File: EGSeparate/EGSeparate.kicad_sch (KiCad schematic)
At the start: 3 parts, among them IC1 PIC16F15325-I_P, IC2 MCP6232-E_P, U1 Opamp_Dual

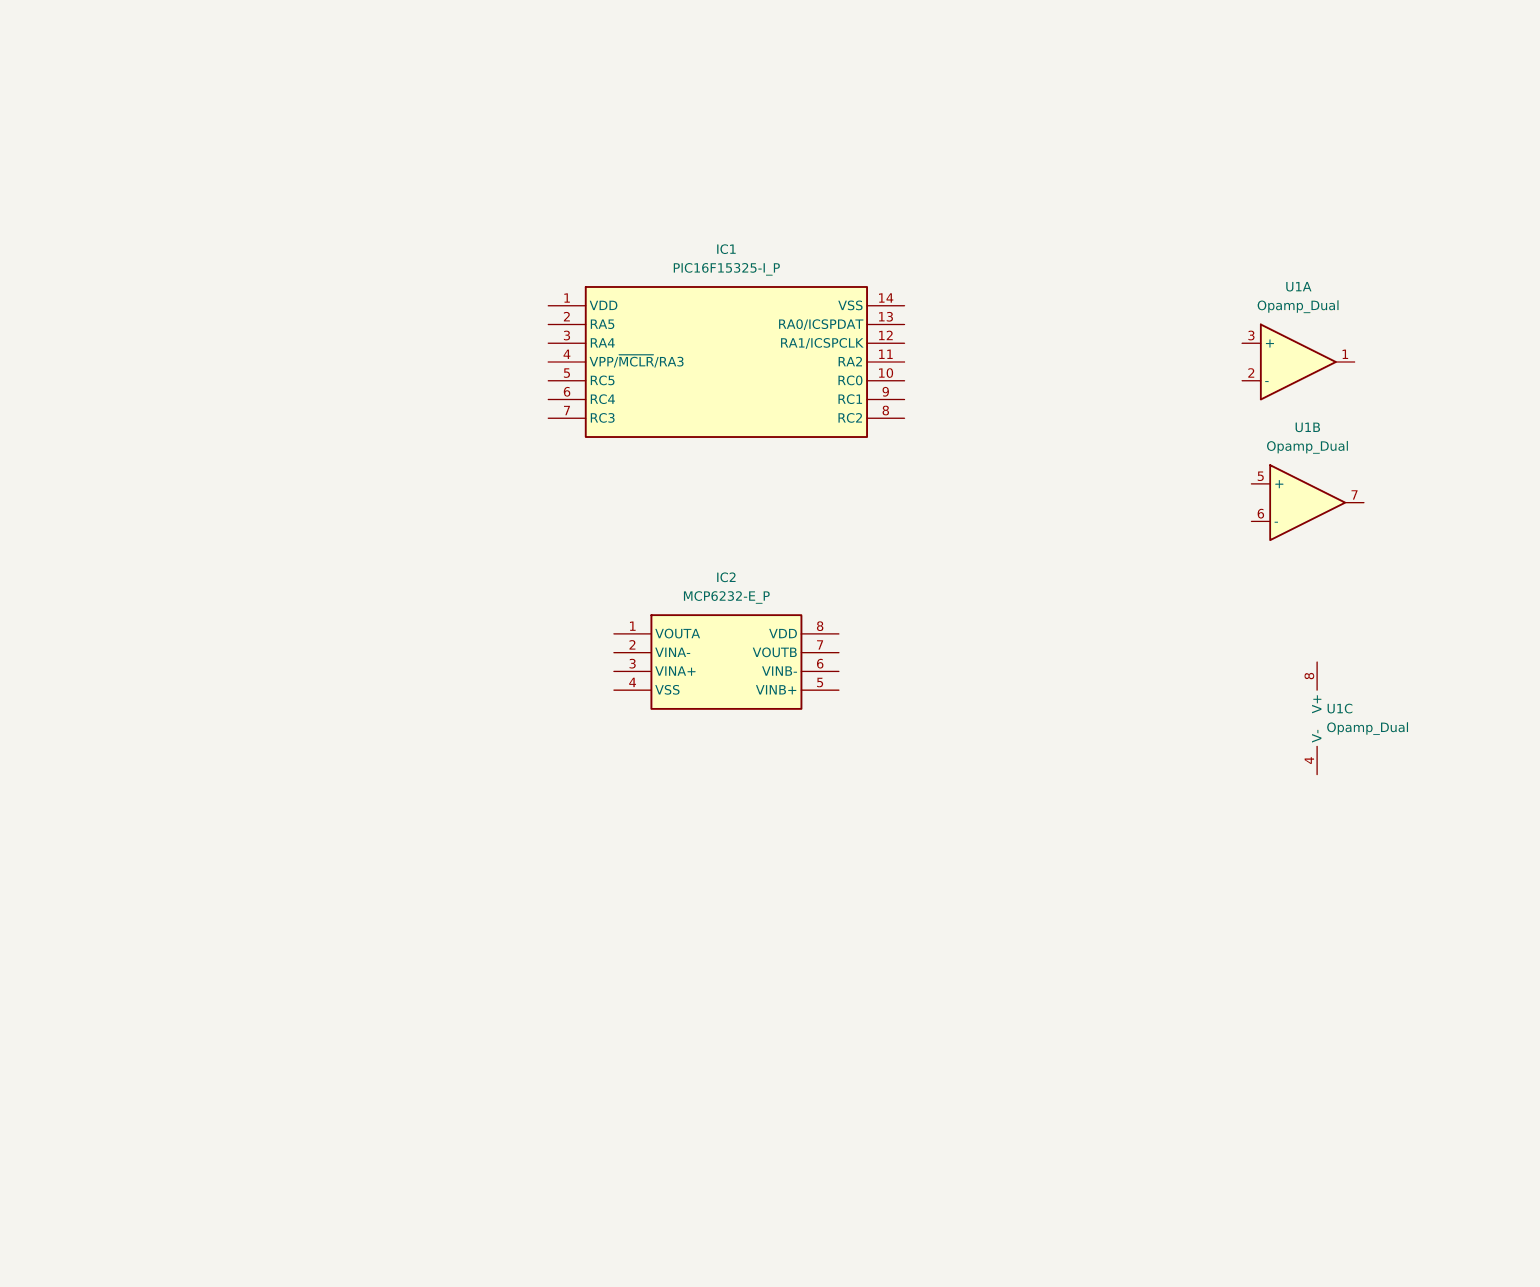
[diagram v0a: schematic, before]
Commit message: LFOSeparate
LFOSeparateは配線完了
EGSeparateは回路図作成中
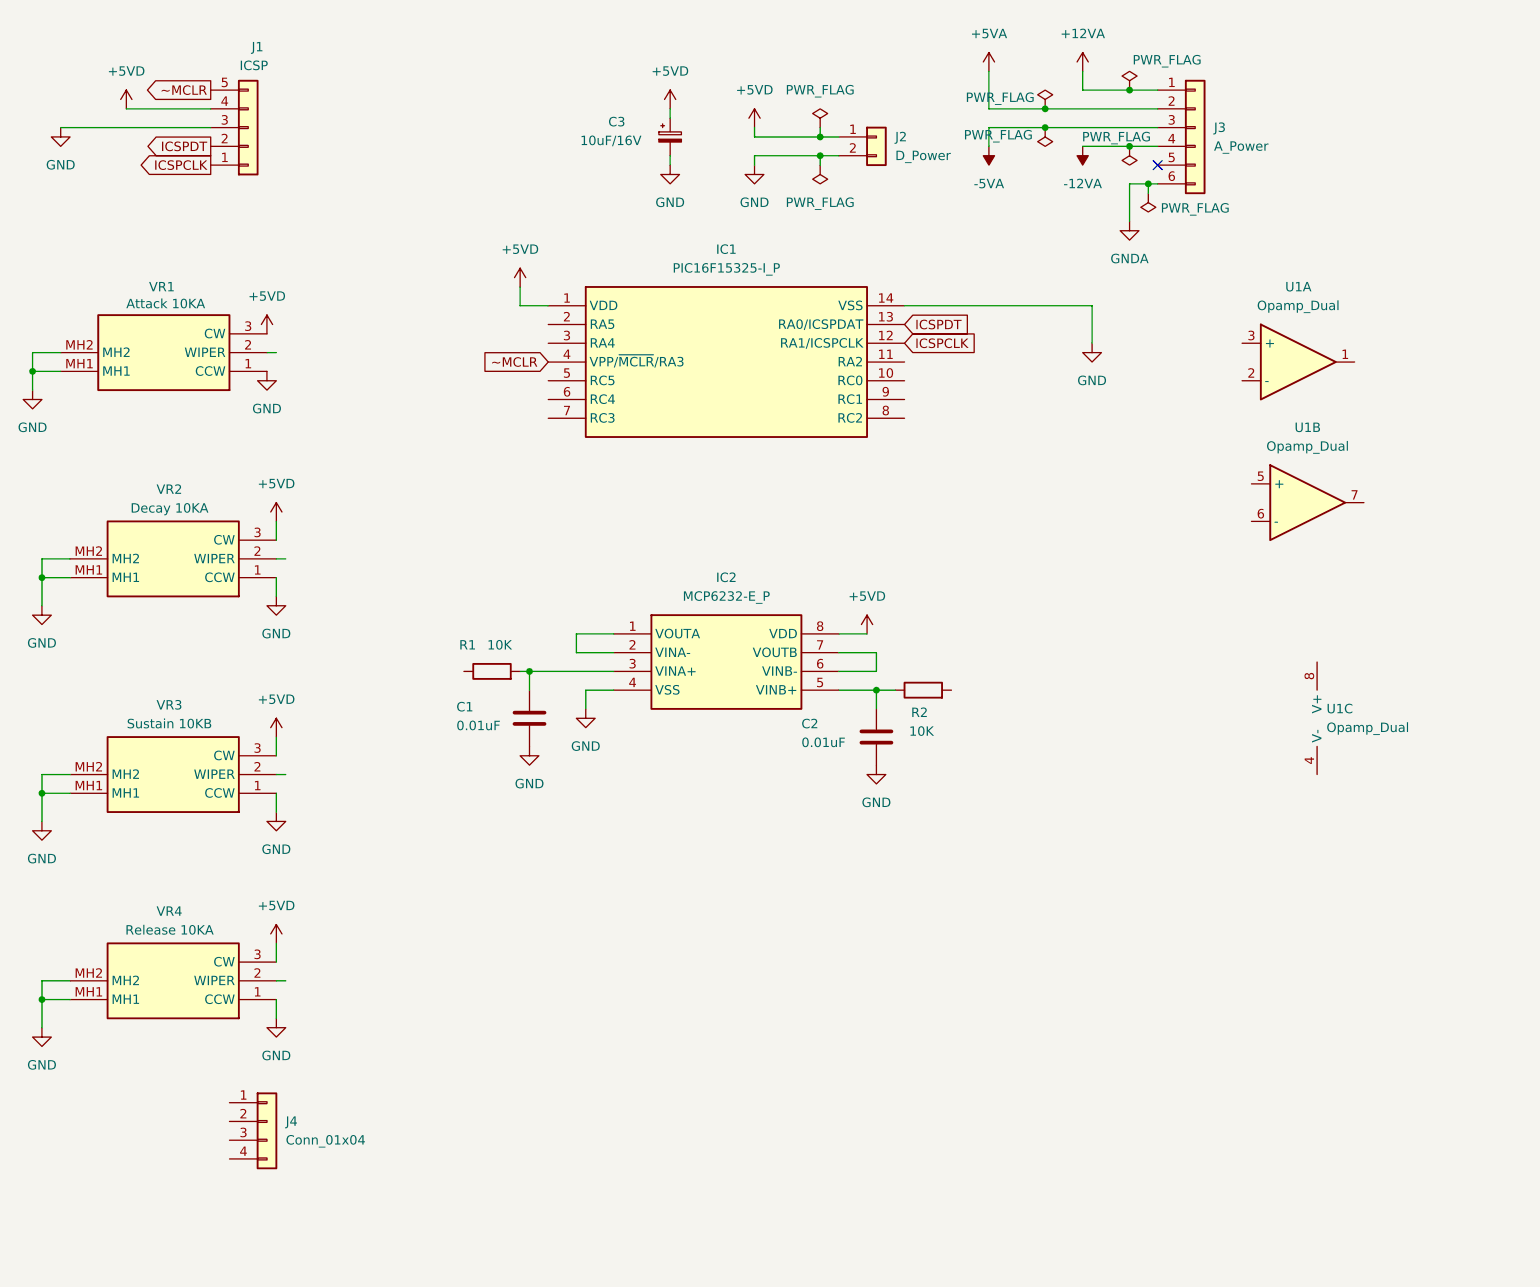
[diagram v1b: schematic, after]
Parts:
- added C1, C2: 0.01uF, Capacitor_THT:C_Disc_D3.4mm_W2.1mm_P2.50mm, symbol Device:C
- added C3: 10uF/16V, Capacitor_THT:CP_Radial_D5.0mm_P2.50mm, symbol Device:C_Polarized_Small
- added J1: ICSP, Connector_PinHeader_2.54mm:PinHeader_1x05_P2.54mm_Horizontal, symbol Connector_Generic:Conn_01x05
- added J2: D_Power, Connector_PinSocket_2.54mm:PinSocket_1x02_P2.54mm_Vertical, symbol Connector_Generic:Conn_01x02
- added J3: A_Power, Connector_PinHeader_2.54mm:PinHeader_1x06_P2.54mm_Vertical, symbol Connector_Generic:Conn_01x06
- added J4: Conn_01x04, Connector_PinHeader_2.54mm:PinHeader_1x04_P2.54mm_Vertical, symbol Connector_Generic:Conn_01x04
- added R1, R2: 10K, Resistor_THT:R_Axial_DIN0204_L3.6mm_D1.6mm_P2.54mm_Vertical, symbol Device:R
- added VR1: Attack 10KA, SamacSys_Parts:RK09D117000B, symbol SamacSys_Parts:RK09D117000B
- added VR2: Decay 10KA, SamacSys_Parts:RK09D117000B, symbol SamacSys_Parts:RK09D117000B
- added VR3: Sustain 10KB, SamacSys_Parts:RK09D117000B, symbol SamacSys_Parts:RK09D117000B
- added VR4: Release 10KA, SamacSys_Parts:RK09D117000B, symbol SamacSys_Parts:RK09D117000B
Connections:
- net at IC2.1 (VOUTA): now also IC2.2 (VINA-)
- net at IC2.3 (VINA+): now also C1.1, R1.2
- net GND: now reaches IC2.4 (VSS)
- net GND: now also IC1.14 (VSS), C1.2, C2.2, C3.2, J1.3 (Pin_3), J2.2 (Pin_2), VR1.1 (CCW), VR1.MH1, VR1.MH2, VR2.1 (CCW), VR2.MH1, VR2.MH2, VR3.1 (CCW), VR3.MH1, VR3.MH2, VR4.1 (CCW), VR4.MH1, VR4.MH2
- net at IC2.5 (VINB+): now also C2.1, R2.1
- net at IC2.6 (VINB-): now also IC2.7 (VOUTB)
- net +5VD: now reaches IC2.8 (VDD)
- net +5VD: now also IC1.1 (VDD), C3.1, J1.4 (Pin_4), J2.1 (Pin_1), VR1.3 (CW), VR2.3 (CW), VR3.3 (CW), VR4.3 (CW)
- net ICSPCLK: now reaches IC1.12 (RA1/ICSPCLK)
- net ICSPCLK: now also J1.1 (Pin_1)
- net ICSPDT: now reaches IC1.13 (RA0/ICSPDAT)
- net ICSPDT: now also J1.2 (Pin_2)
- net ~MCLR: now reaches IC1.4 (VPP/~{MCLR}/RA3)
- net ~MCLR: now also J1.5 (Pin_5)
- new net +12VA: J3.1 (Pin_1)
- new net +5VA: J3.2 (Pin_2)
- new net -12VA: J3.4 (Pin_4)
- new net -5VA: J3.3 (Pin_3)
- new net GNDA: J3.6 (Pin_6)
- no-connect marks 0 -> 1

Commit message: EGSeparate
配線完了　シルク未記入
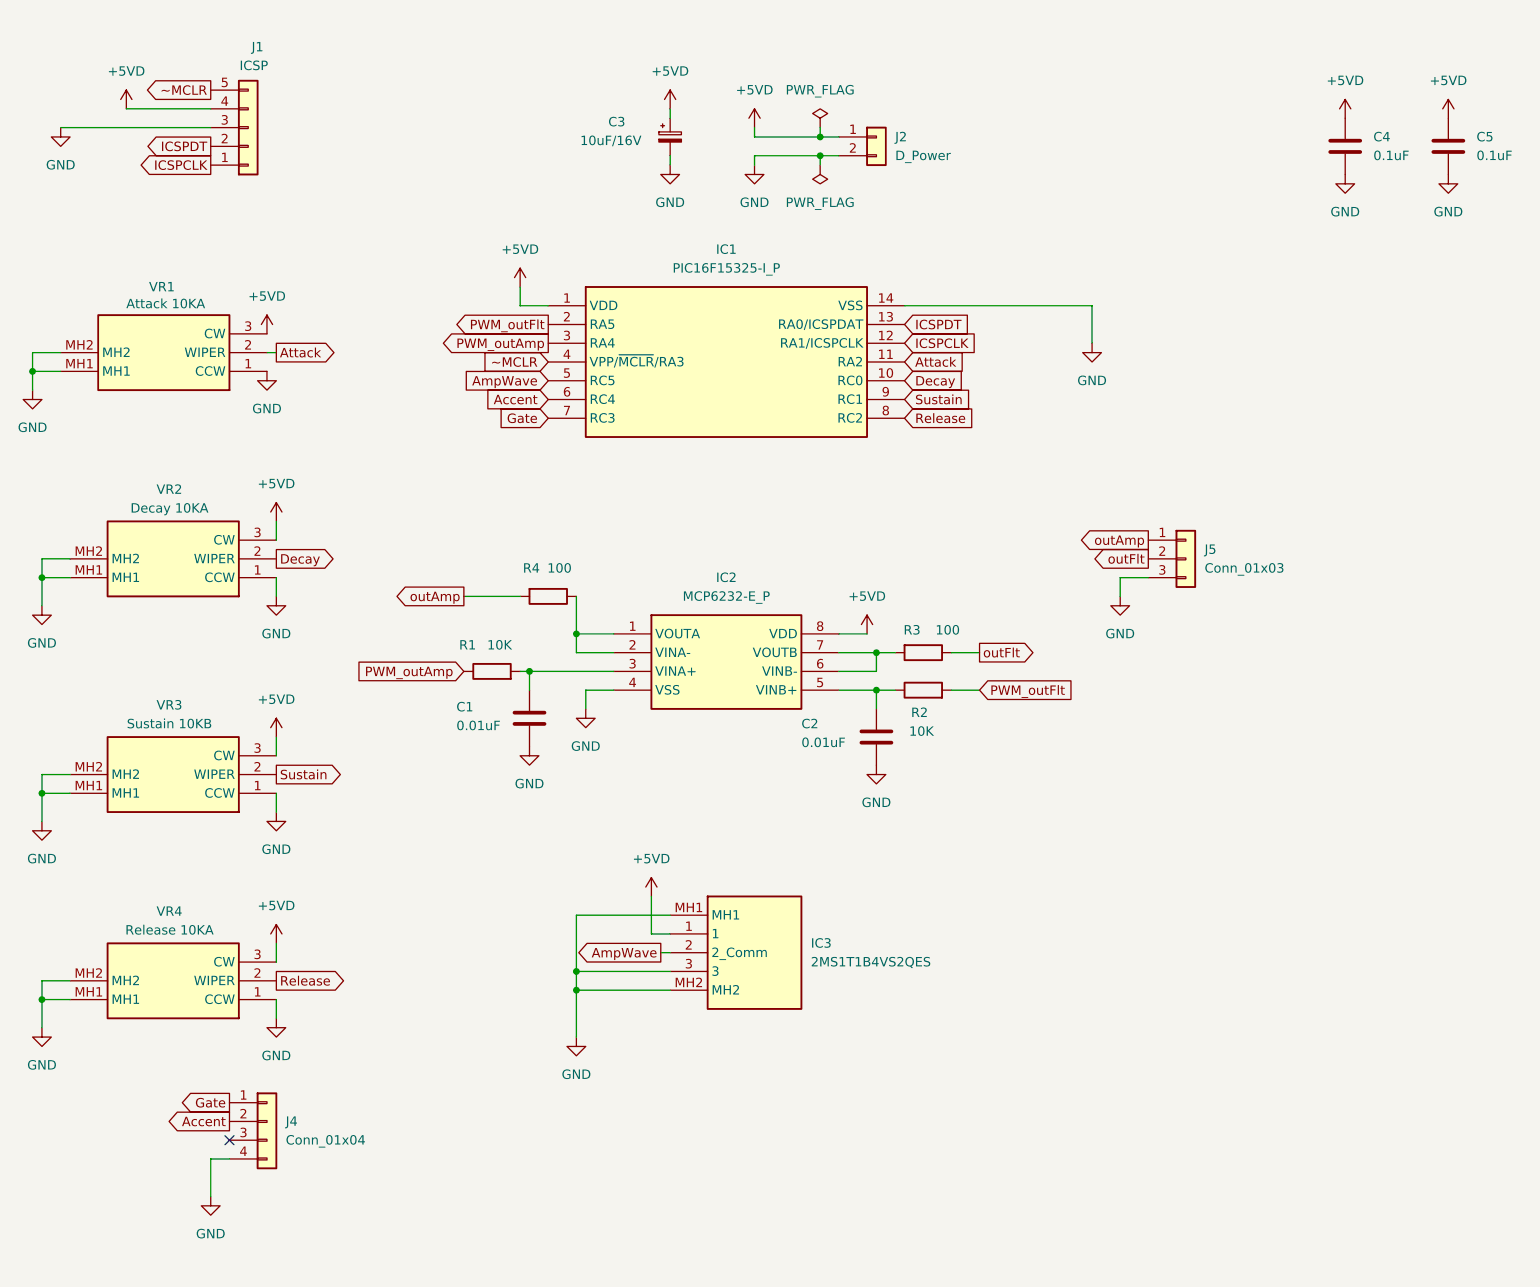
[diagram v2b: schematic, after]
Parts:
- removed J3: A_Power, Connector_PinHeader_2.54mm:PinHeader_1x06_P2.54mm_Vertical, symbol Connector_Generic:Conn_01x06
- removed U1: Opamp_Dual, Package_DIP:DIP-8_W7.62mm_LongPads, symbol Device:Opamp_Dual
- added C4, C5: 0.1uF, Capacitor_SMD:C_0805_2012Metric_Pad1.18x1.45mm_HandSolder, symbol Device:C
- added IC3: 2MS1T1B4VS2QES, 2MS1T1B4VS2QES, symbol SamacSys_Parts:2MS1T1B4VS2QES
- added J5: Conn_01x03, Connector_PinHeader_2.54mm:PinHeader_1x03_P2.54mm_Vertical, symbol Connector_Generic:Conn_01x03
- added R3, R4: 100, Resistor_THT:R_Axial_DIN0204_L3.6mm_D1.6mm_P2.54mm_Vertical, symbol Device:R
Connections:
- net +5VD: now also C4.1, C5.1, IC3.1
- net GND: now also J4.4 (Pin_4), C4.2, C5.2, IC3.3, IC3.MH1, IC3.MH2, J5.3 (Pin_3)
- net Release: now reaches VR4.2 (WIPER)
- net Release: now also IC1.8 (RC2)
- net PWM_outFlt: now reaches R2.2
- net PWM_outFlt: now also IC1.2 (RA5)
- net Sustain: now reaches VR3.2 (WIPER)
- net Sustain: now also IC1.9 (RC1)
- net at IC2.1 (VOUTA), IC2.2 (VINA-): now also R4.1
- net at IC2.6 (VINB-), IC2.7 (VOUTB): now also R3.2
- net Attack: now reaches VR1.2 (WIPER)
- net Attack: now also IC1.11 (RA2)
- net Decay: now reaches VR2.2 (WIPER)
- net Decay: now also IC1.10 (RC0)
- net Gate: now reaches J4.1 (Pin_1)
- net Gate: now also IC1.7 (RC3)
- net Accent: now reaches J4.2 (Pin_2)
- net Accent: now also IC1.6 (RC4)
- net PWM_outAmp: now reaches IC1.3 (RA4)
- net PWM_outAmp: now also R1.1
- net AmpWave: now reaches IC1.5 (RC5)
- net AmpWave: now also IC3.2 (2_Comm)
- new net outAmp: J5.1 (Pin_1), R4.2
- new net outFlt: J5.2 (Pin_2), R3.1

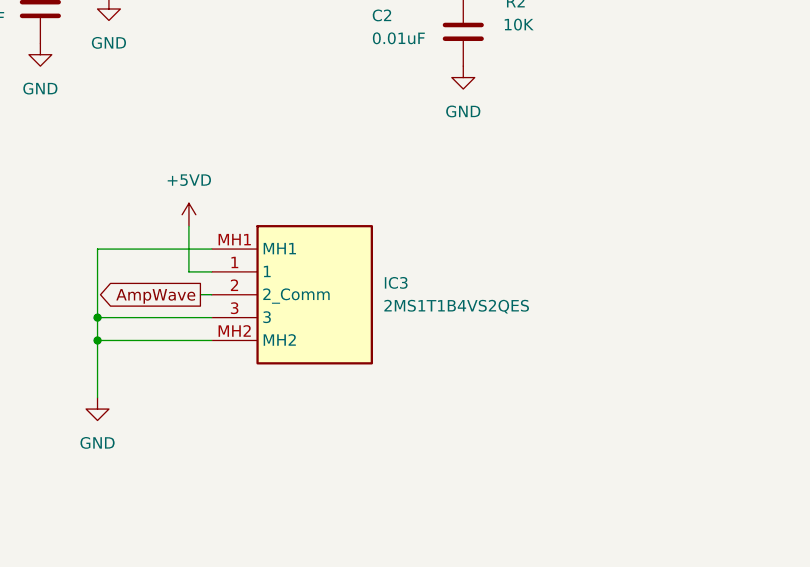
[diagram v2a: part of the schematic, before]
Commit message: EGSeparate
シルクスクリーンに説明文を追記
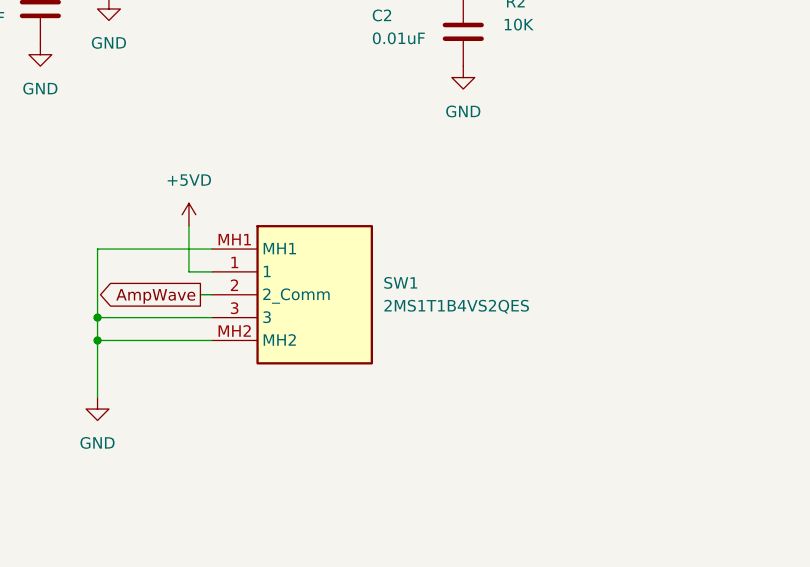
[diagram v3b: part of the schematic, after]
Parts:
- renumbered IC3 to SW1
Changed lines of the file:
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@@
 		(dnp no)
 		(fields_autoplaced yes)
-		(property "Reference" "IC3"
+		(property "Reference" "SW1"
 			(at 139.7 142.2399 0)
 			(effects
@@
 			(project ""
 				(path "/b7fa371b-9510-43de-8615-2bc962502cbb"
-					(reference "IC3")
+					(reference "SW1")
 					(unit 1)
 				)
